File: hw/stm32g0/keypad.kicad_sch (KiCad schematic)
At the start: 14 parts, among them SW401 SW_Push, SW402 SW_Push, SW403 SW_Push, SW404 SW_Push, SW405 SW_Push, SW406 SW_Push, U401 4050

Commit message: chore(hw): update title blocks
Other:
- company: (none) -> Stefan Misik
- title: (none) -> STM32G0 LED Controller
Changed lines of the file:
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@@
 	(generator_version "8.0")
 	(paper "A4")
+	(title_block
+		(title "STM32G0 LED Controller")
+		(date "2024-06-29")
+		(company "Stefan Misik")
+		(comment 1 "www.stefanmisik.com")
+	)
 	(junction
 		(at 129.54 97.79)

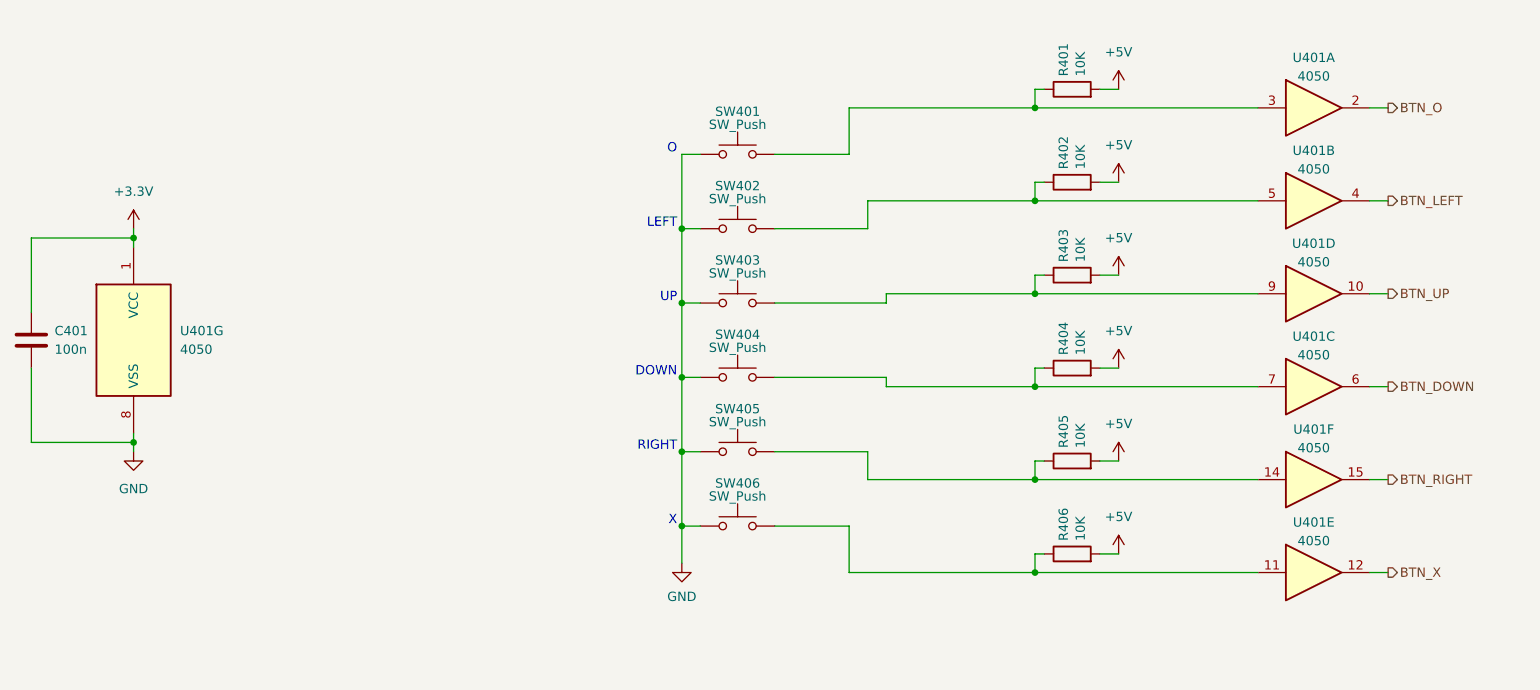
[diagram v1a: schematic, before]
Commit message: chore(hw): add keypad ESD protection
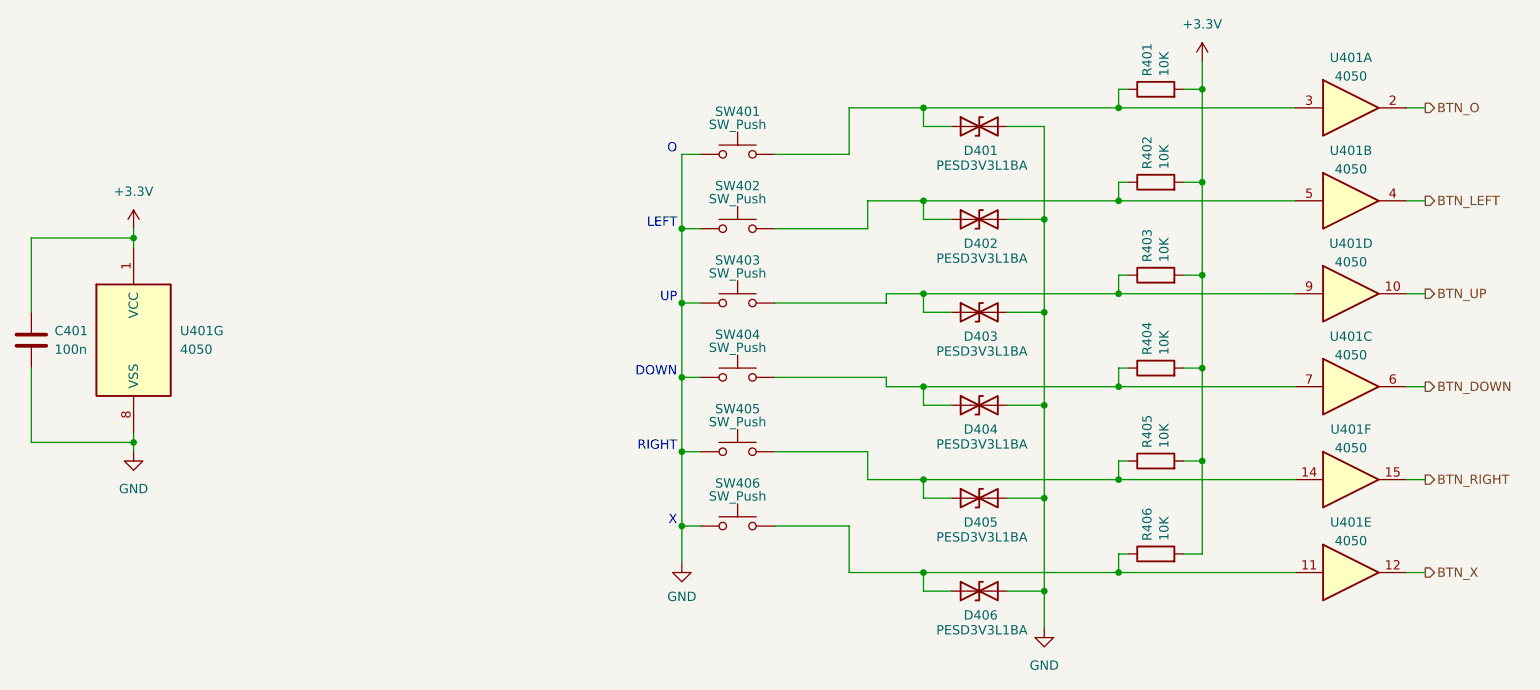
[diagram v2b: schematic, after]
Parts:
- added D401, D402, D403, D404, D405, D406: PESD3V3L1BA, Diode_SMD:D_SOD-323_HandSoldering, symbol Device:D_TVS
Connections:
- net +5V is gone; now on net +3.3V: R401.2, R402.2, R403.2, R404.2, R405.2, R406.2
- net GND: now also D401.2 (A2), D402.2 (A2), D403.2 (A2), D404.2 (A2), D405.2 (A2), D406.2 (A2)
- net at R403.1, SW403.2, U401.9: now also D403.1 (A1)
- net at R402.1, SW402.2, U401.5: now also D402.1 (A1)
- net at R406.1, SW406.2, U401.11: now also D406.1 (A1)
- net at R401.1, SW401.2, U401.3: now also D401.1 (A1)
- net at R405.1, SW405.2, U401.14: now also D405.1 (A1)
- net at R404.1, SW404.2, U401.7: now also D404.1 (A1)
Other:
- moved on the sheet: R401, R402, R403, R404, R405, R406, U401A, U401B, U401C, U401D, U401E, U401F
